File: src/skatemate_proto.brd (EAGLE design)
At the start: 160 x 100 mm, 101 parts, among them IC1 REG1117, Q1 IRF740, Q2 IRF740, Q3 IRF740, Q4 IRF740, Q5 IRF740, Q6 IRF740, U1 DRV8301DCAR

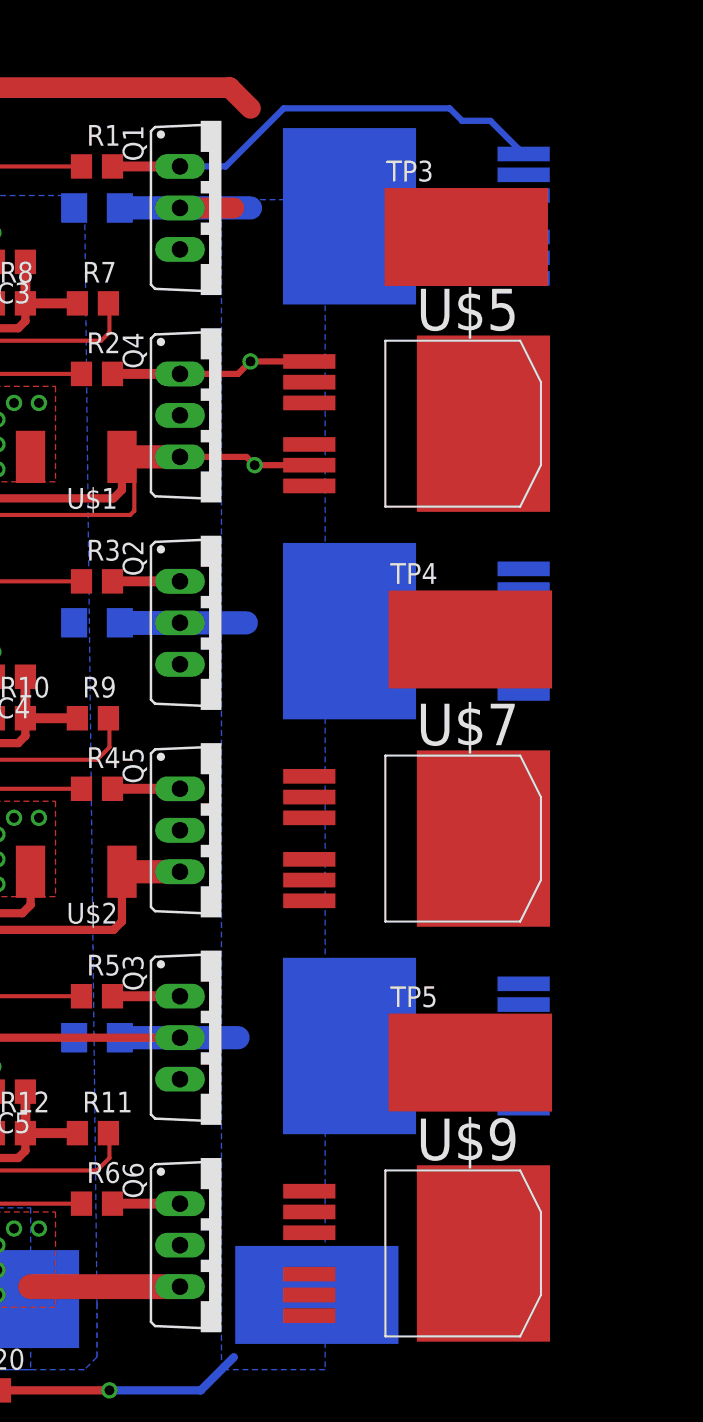
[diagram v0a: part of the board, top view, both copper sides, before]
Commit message: Layout_Testplatine_fertig_1
FET's zusätzlich verbunden
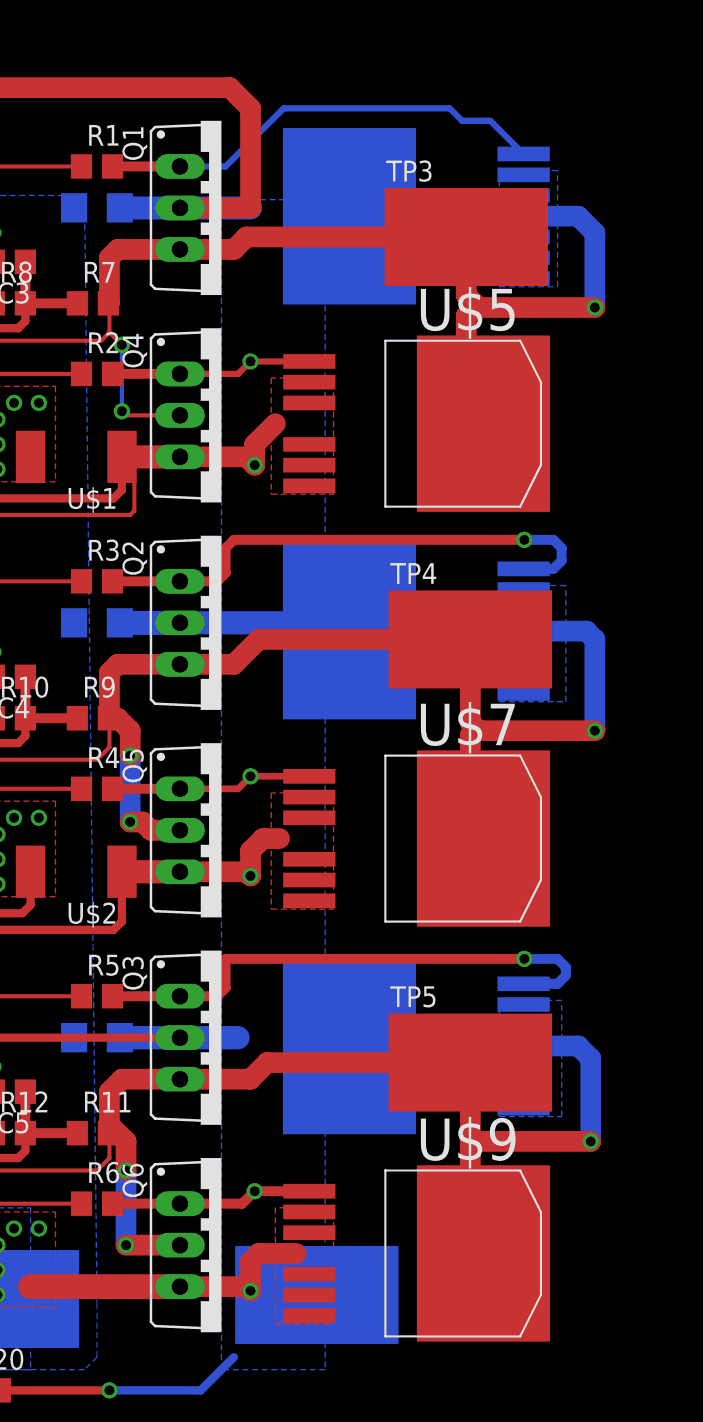
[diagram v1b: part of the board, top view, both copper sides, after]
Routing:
- net PH_B: track 26.8 -> 93.3 mm, vias 0 -> 3
- net PH_C: track 47.2 -> 112.2 mm, vias 0 -> 3
- net PH_A: track 44.5 -> 107.5 mm, vias 0 -> 3
- net N$11: track 4.13 -> 33.3 mm, vias 0 -> 1
- net N$10: track 4.13 -> 33.0 mm, vias 0 -> 1
- net SUPPLY: track 148.9 -> 162.8 mm
- net GND: track 246.5 -> 255.7 mm, vias 34 -> 35
- net N$9: track 4.13 -> 12.4 mm, vias 0 -> 1
- net N$12: track 4.13 -> 12.4 mm, vias 0 -> 1
- net SN_B: track 59.8 -> 67.9 mm
- added copper zone on layer 16, net PH_A
- added copper zone on layer 16, net PH_B
- added copper zone on layer 16, net PH_C
- added copper zone on layer 1, net SN_A
- added copper zone on layer 1, net SN_B

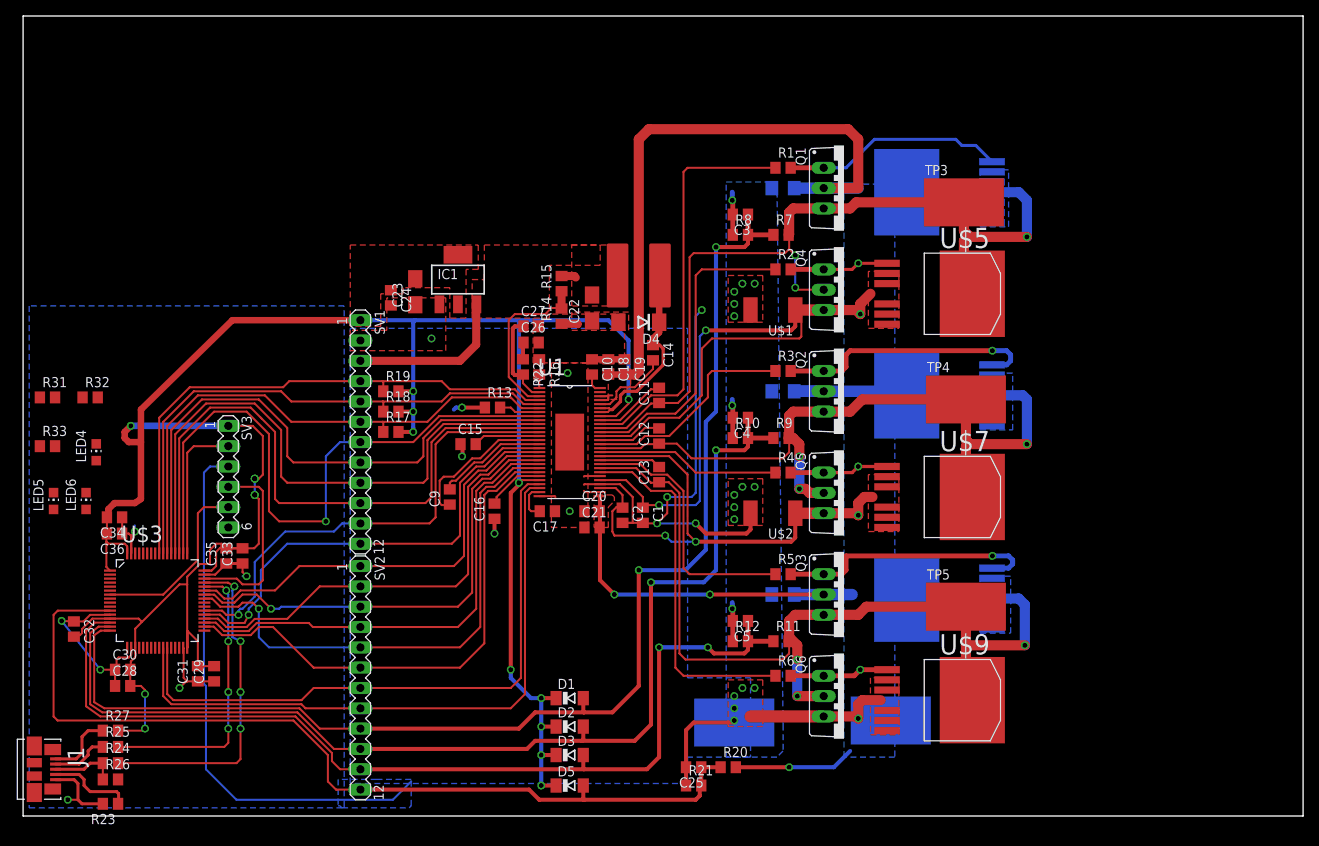
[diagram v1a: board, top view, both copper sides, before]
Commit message: Added LED and crystal
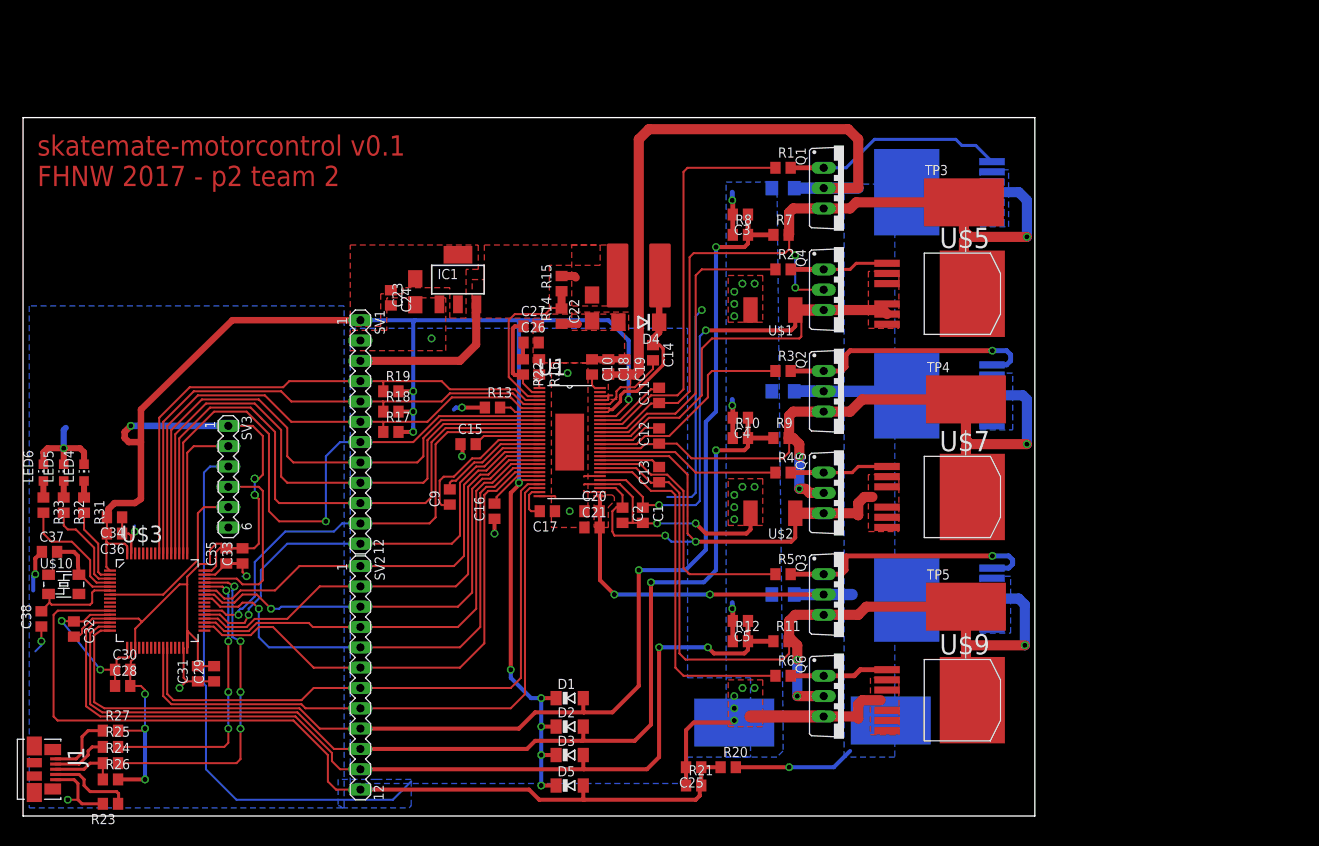
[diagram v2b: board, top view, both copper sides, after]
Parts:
- added C37, C38: 22p, skatemate:C0805
- added U$10: ABM3B, skatemate:IQG5032B
- moved R31 14.2 mm to (7.62, 38.9), turned to 270 degrees
- moved R32 13.9 mm to (5.08, 38.9), turned to 270 degrees
- moved R33 7.38 mm to (2.54, 38.9), turned to 270 degrees
- moved LED6 6.41 mm to (2.54, 42.9)
- moved LED5 3.78 mm to (5.08, 42.9)
- moved LED4 2.96 mm to (7.62, 42.9)
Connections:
- new net N$28: R33.2, U$3.4
- new net N$29: R32.2, U$3.3
- new net N$30: R31.2, U$3.2
- new net N$31: LED4.A, R31.1
- new net N$32: LED5.A, R32.1
- new net N$33: LED6.A, R33.1
- new net N$35: C38.2, U$10.1, U$3.6
- new net N$36: C37.2, U$10.3, U$3.5
- net GND: now also C37.1, C38.1, LED4.C, LED5.C, LED6.C
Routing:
- net GND: track 255.7 -> 273.7 mm, vias 35 -> 36
- net N$28: track 0.00 -> 14.7 mm, vias 1 -> 0
- net N$29: track 0.00 -> 12.1 mm
- net N$35: track 0.00 -> 11.8 mm
- net N$36: track 0.00 -> 10.2 mm
- net N$30: track 0.00 -> 9.76 mm
- net VCC: track 308.1 -> 317.3 mm, vias 15 -> 16
- net N$33: track 0.00 -> 2.06 mm
- net N$32: track 0.00 -> 2.06 mm
- net N$31: track 0.00 -> 2.06 mm
- net PH_C: track 112.2 -> 113.0 mm
- net N$8: track 12.4 -> 12.9 mm, vias 1 -> 0
- net SN_A: track 98.8 -> 99.1 mm, vias 3 -> 2
- net N$9: vias 1 -> 0
- net N$12: vias 1 -> 0
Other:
- board size 160 x 100 mm -> 126.5 x 87.3 mm
- board text added: "FHNW 2017 - p2 team 2"
- board text added: "skatemate-motorcontrol v0.1"
